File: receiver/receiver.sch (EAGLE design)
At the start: 9 parts, among them P1 PROMICRO_HEADER, P2 PROMICRO_HEADER, U1 CORE51822B, U2 3.3

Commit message: update board
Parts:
- U2: value 3.3 -> AZ1117IH; device adafruit:MOSFET-NREFLOW -> az1117ih:AZ1117IH
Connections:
- net GND: now also U2.ADJ/GND; no longer U2.G
- net VCC: now also U2.OUTPUT, U2.VOUT; no longer U2.S
- net VIN: now also U2.INPUT; no longer U2.D
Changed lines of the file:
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@@
 </classes>
 <parts>
-<part name="U2" library="adafruit" deviceset="MOSFET-N" device="REFLOW" value="3.3"/>
 <part name="GND1" library="supply1" library_urn="urn:adsk.eagle:library:371" deviceset="GND" device=""/>
 <part name="GND2" library="supply1" library_urn="urn:adsk.eagle:library:371" deviceset="GND" device=""/>
@@
 <part name="P2" library="promicro_header" deviceset="PROMICRO_HEADER" device=""/>
 <part name="P1" library="promicro_header" deviceset="PROMICRO_HEADER" device=""/>
+<part name="U2" library="az1117ih" deviceset="AZ1117IH" device=""/>
 </parts>
 <sheets>
@@
 </plain>
 <instances>
-<instance part="U2" gate="G$1" x="96.52" y="119.38" rot="R90"/>
-<instance part="GND1" gate="1" x="99.06" y="111.76"/>
+<instance part="GND1" gate="1" x="124.46" y="104.14"/>
 <instance part="GND2" gate="1" x="68.58" y="116.84" rot="R90"/>
 <instance part="GND3" gate="1" x="-20.32" y="76.2"/>
 <instance part="GND4" gate="1" x="30.48" y="109.22" rot="R90"/>
-<instance part="P+1" gate="VCC" x="106.68" y="121.92" rot="R270"/>
+<instance part="P+1" gate="VCC" x="96.52" y="111.76" rot="R90"/>
 <instance part="D1" gate="G$1" x="119.38" y="27.94"/>
 <instance part="RA2" gate="G$1" x="71.12" y="-2.54"/>
@@
 <instance part="P2" gate="G$1" x="53.34" y="109.22"/>
 <instance part="P1" gate="G$1" x="10.16" y="109.22"/>
+<instance part="U2" gate="G$1" x="116.84" y="111.76"/>
 </instances>
 <busses>
@@
 <nets>
 <net name="GND" class="0">
-<segment>
-<pinref part="GND1" gate="1" pin="GND"/>
-<pinref part="U2" gate="G$1" pin="G"/>
-<wire x1="99.06" y1="114.3" x2="99.06" y2="116.84" width="0.1524" layer="91"/>
-</segment>
 <segment>
 <pinref part="GND2" gate="1" pin="GND"/>
@@
 <junction x="22.86" y="109.22"/>
 </segment>
+<segment>
+<pinref part="U2" gate="G$1" pin="ADJ/GND"/>
+<pinref part="GND1" gate="1" pin="GND"/>
+<wire x1="124.46" y1="109.22" x2="119.38" y2="109.22" width="0.1524" layer="91"/>
+<wire x1="124.46" y1="109.22" x2="124.46" y2="106.68" width="0.1524" layer="91"/>
+</segment>
 </net>
 <net name="VCC" class="0">
-<segment>
-<pinref part="U2" gate="G$1" pin="S"/>
-<pinref part="P+1" gate="VCC" pin="VCC"/>
-<wire x1="101.6" y1="121.92" x2="104.14" y2="121.92" width="0.1524" layer="91"/>
-</segment>
 <segment>
 <pinref part="U1" gate="G$1" pin="VCC"/>
@@
 <wire x1="10.16" y1="33.02" x2="2.54" y2="33.02" width="0.1524" layer="91"/>
 <wire x1="2.54" y1="33.02" x2="2.54" y2="27.94" width="0.1524" layer="91"/>
+</segment>
+<segment>
+<pinref part="U2" gate="G$1" pin="VOUT"/>
+<pinref part="P+1" gate="VCC" pin="VCC"/>
+<wire x1="114.3" y1="111.76" x2="99.06" y2="111.76" width="0.1524" layer="91"/>
+<pinref part="U2" gate="G$1" pin="OUTPUT"/>
+<wire x1="119.38" y1="111.76" x2="99.06" y2="111.76" width="0.1524" layer="91"/>
+<junction x="99.06" y="111.76"/>
 </segment>
 </net>
@@
 </segment>
 <segment>
-<pinref part="U2" gate="G$1" pin="D"/>
-<wire x1="91.44" y1="121.92" x2="86.36" y2="121.92" width="0.1524" layer="91"/>
-<label x="81.28" y="121.92" size="1.778" layer="95"/>
-</segment>
-<segment>
 <pinref part="D1" gate="G$1" pin="COMM(ANODE)"/>
 <wire x1="111.76" y1="25.4" x2="106.68" y2="25.4" width="0.1524" layer="91"/>
@@
 <label x="104.14" y="15.24" size="1.778" layer="95"/>
 </segment>
-</net>
+<segment>
+<pinref part="U2" gate="G$1" pin="INPUT"/>
+<wire x1="119.38" y1="114.3" x2="124.46" y2="114.3" width="0.1524" layer="91"/>
+<wire x1="124.46" y1="114.3" x2="124.46" y2="116.84" width="0.1524" layer="91"/>
+<label x="124.46" y="116.84" size="1.778" layer="95"/>
+</segment>
+</net>

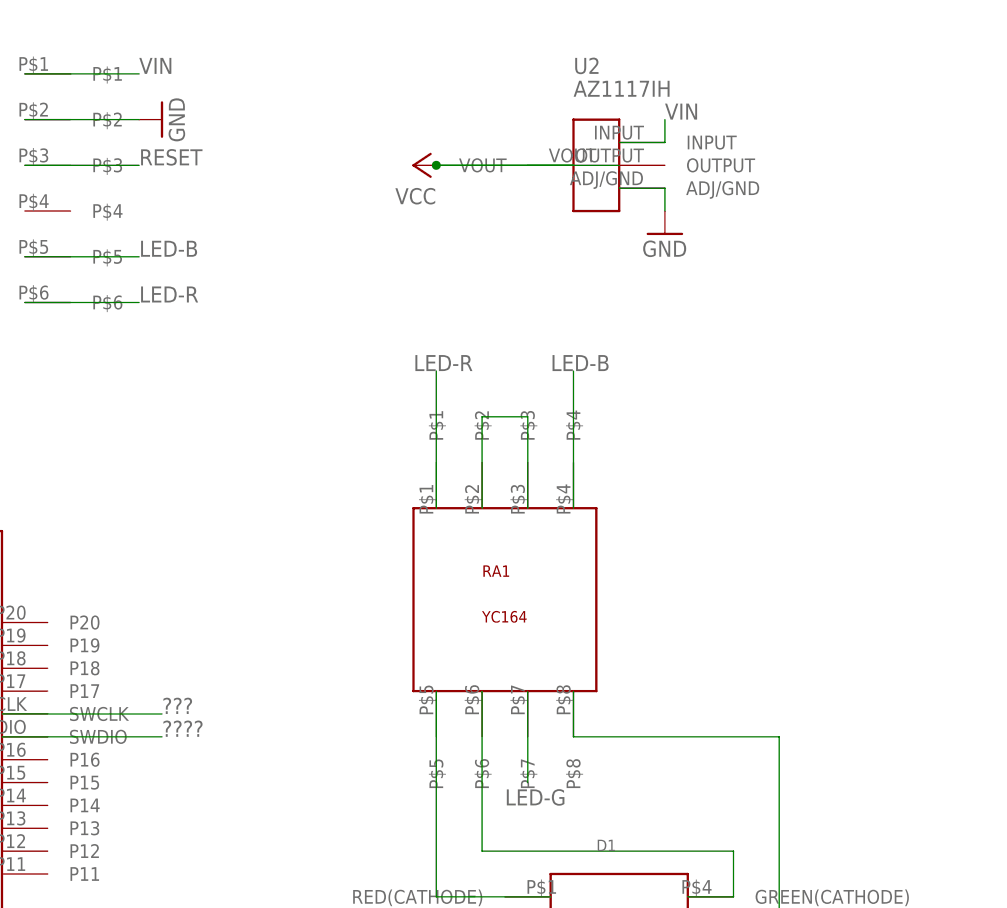
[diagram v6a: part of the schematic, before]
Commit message: include programming header on board
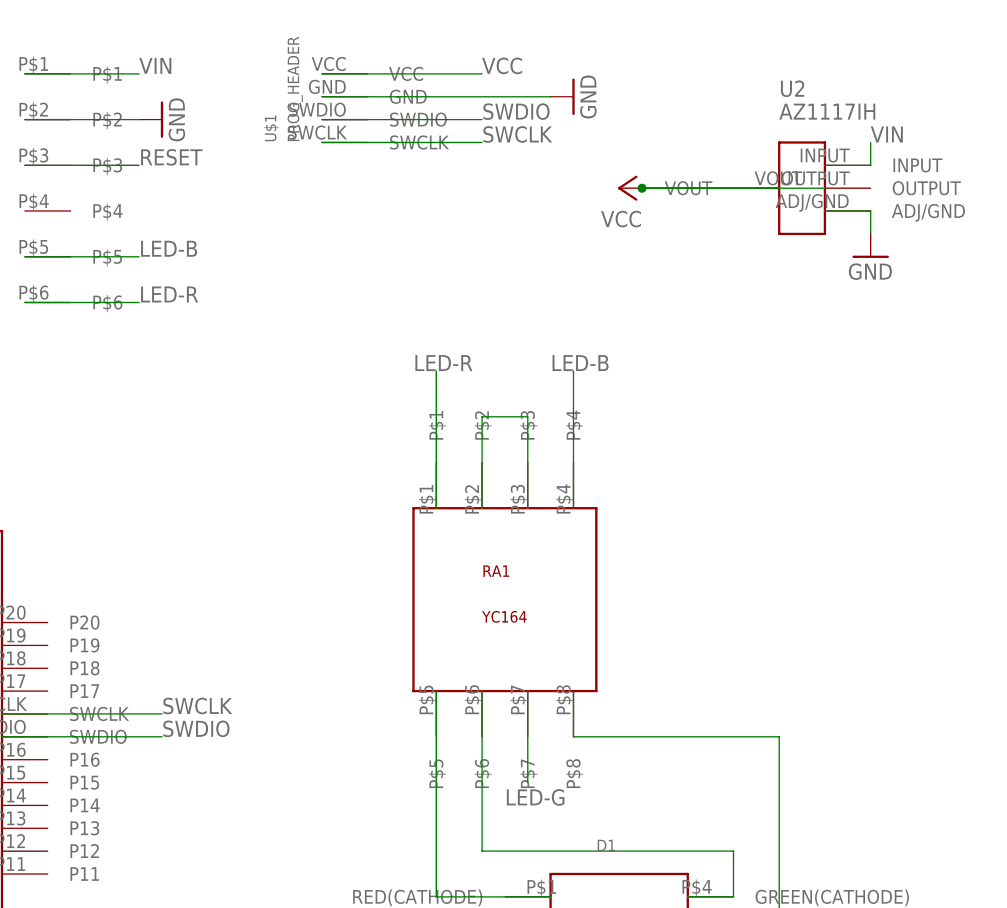
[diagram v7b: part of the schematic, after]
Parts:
- added U$1: PROG_HEADER, prog_header:PROG_HEADER
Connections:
- removed net ???: U1.SWCLK
- removed net ????: U1.SWDIO
- new net SWCLK: U$1.SWCLK, U1.SWCLK
- new net SWDIO: U$1.SWDIO, U1.SWDIO
- net GND: now also U$1.GND
- net VCC: now also U$1.VCC
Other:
- moved on the sheet: U2
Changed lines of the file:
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@@
 <part name="P1" library="promicro_header" deviceset="PROMICRO_HEADER" device=""/>
 <part name="U2" library="az1117ih" deviceset="AZ1117IH" device=""/>
+<part name="U$1" library="prog_header" deviceset="PROG_HEADER" device=""/>
+<part name="GND5" library="supply1" library_urn="urn:adsk.eagle:library:371" deviceset="GND" device=""/>
 </parts>
 <sheets>
@@
 </plain>
 <instances>
-<instance part="GND1" gate="1" x="124.46" y="104.14"/>
+<instance part="GND1" gate="1" x="147.32" y="101.6"/>
 <instance part="GND2" gate="1" x="68.58" y="116.84" rot="R90"/>
 <instance part="GND3" gate="1" x="-20.32" y="76.2"/>
 <instance part="GND4" gate="1" x="30.48" y="109.22" rot="R90"/>
-<instance part="P+1" gate="VCC" x="96.52" y="111.76" rot="R90"/>
+<instance part="P+1" gate="VCC" x="119.38" y="109.22" rot="R90"/>
 <instance part="D1" gate="G$1" x="119.38" y="27.94"/>
 <instance part="RA2" gate="G$1" x="71.12" y="-2.54"/>
@@
 <instance part="P2" gate="G$1" x="53.34" y="109.22"/>
 <instance part="P1" gate="G$1" x="10.16" y="109.22"/>
-<instance part="U2" gate="G$1" x="116.84" y="111.76"/>
+<instance part="U2" gate="G$1" x="139.7" y="109.22"/>
+<instance part="U$1" gate="G$1" x="86.36" y="121.92"/>
+<instance part="GND5" gate="1" x="114.3" y="119.38" rot="R90"/>
 </instances>
 <busses>
@@
 <pinref part="U2" gate="G$1" pin="ADJ/GND"/>
 <pinref part="GND1" gate="1" pin="GND"/>
-<wire x1="124.46" y1="109.22" x2="119.38" y2="109.22" width="0.1524" layer="91"/>
-<wire x1="124.46" y1="109.22" x2="124.46" y2="106.68" width="0.1524" layer="91"/>
+<wire x1="147.32" y1="106.68" x2="142.24" y2="106.68" width="0.1524" layer="91"/>
+<wire x1="147.32" y1="106.68" x2="147.32" y2="104.14" width="0.1524" layer="91"/>
+</segment>
+<segment>
+<pinref part="U$1" gate="G$1" pin="GND"/>
+<wire x1="86.36" y1="119.38" x2="111.76" y2="119.38" width="0.1524" layer="91"/>
+<pinref part="GND5" gate="1" pin="GND"/>
 </segment>
 </net>
@@
 <pinref part="U2" gate="G$1" pin="VOUT"/>
 <pinref part="P+1" gate="VCC" pin="VCC"/>
-<wire x1="114.3" y1="111.76" x2="99.06" y2="111.76" width="0.1524" layer="91"/>
+<wire x1="137.16" y1="109.22" x2="121.92" y2="109.22" width="0.1524" layer="91"/>
 <pinref part="U2" gate="G$1" pin="OUTPUT"/>
-<wire x1="119.38" y1="111.76" x2="99.06" y2="111.76" width="0.1524" layer="91"/>
-<junction x="99.06" y="111.76"/>
+<wire x1="142.24" y1="109.22" x2="121.92" y2="109.22" width="0.1524" layer="91"/>
+<junction x="121.92" y="109.22"/>
+</segment>
+<segment>
+<pinref part="U$1" gate="G$1" pin="VCC"/>
+<wire x1="86.36" y1="121.92" x2="104.14" y2="121.92" width="0.1524" layer="91"/>
+<label x="104.14" y="121.92" size="1.778" layer="95"/>
 </segment>
 </net>
@@
 <segment>
 <pinref part="U2" gate="G$1" pin="INPUT"/>
-<wire x1="119.38" y1="114.3" x2="124.46" y2="114.3" width="0.1524" layer="91"/>
-<wire x1="124.46" y1="114.3" x2="124.46" y2="116.84" width="0.1524" layer="91"/>
-<label x="124.46" y="116.84" size="1.778" layer="95"/>
+<wire x1="142.24" y1="111.76" x2="147.32" y2="111.76" width="0.1524" layer="91"/>
+<wire x1="147.32" y1="111.76" x2="147.32" y2="114.3" width="0.1524" layer="91"/>
+<label x="147.32" y="114.3" size="1.778" layer="95"/>
 </segment>
 </net>
@@
 </segment>
 </net>
-<net name="???" class="0">
+<net name="SWCLK" class="0">
 <segment>
 <pinref part="U1" gate="G$1" pin="SWCLK"/>
@@
 <label x="68.58" y="50.8" size="1.778" layer="95"/>
 </segment>
-</net>
-<net name="????" class="0">
+<segment>
+<pinref part="U$1" gate="G$1" pin="SWCLK"/>
+<wire x1="86.36" y1="114.3" x2="104.14" y2="114.3" width="0.1524" layer="91"/>
+<label x="104.14" y="114.3" size="1.778" layer="95"/>
+</segment>
+</net>
+<net name="SWDIO" class="0">
+<segment>
+<pinref part="U$1" gate="G$1" pin="SWDIO"/>
+<wire x1="86.36" y1="116.84" x2="104.14" y2="116.84" width="0.1524" layer="91"/>
+<label x="104.14" y="116.84" size="1.778" layer="95"/>
+</segment>
 <segment>
 <pinref part="U1" gate="G$1" pin="SWDIO"/>
